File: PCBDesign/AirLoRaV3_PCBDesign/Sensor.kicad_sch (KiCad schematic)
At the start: 11 parts, among them J3 UART2, J4 UART2, J5 UART2, Q1 S8050, Q2 S8050, Q3 S8050, Q4 S8050, U5 SHT21

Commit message: Update circiut
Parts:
- added R12, R13, R14, R15: 1K, Resistor_SMD:R_0603_1608Metric, symbol Device:R
- C41: footprint (none) -> Capacitor_SMD:C_0603_1608Metric
- R10: renamed from R4; footprint (none) -> Resistor_SMD:R_0603_1608Metric
- R11: renamed from R5; footprint (none) -> Resistor_SMD:R_0603_1608Metric
- U5: footprint SHT21:XDCR_SHT21 -> footprint:XDCR_SHT21
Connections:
- net GND: now also Q1.1 (E); no longer C41.2, U5.2 (VSS)
- net at Q3.2 (B): now also R14.2
- net at Q2.2 (B): now also R13.2
- net at Q2.3 (C): now also J3.2 (Pin_2)
- net at Q1.2 (B): now also R12.1
- net at Q1.3 (C): now also C41.2, U5.2 (VSS)
- net at Q4.2 (B): now also R15.2
- net 3.3V renamed +3.3V
- net 5V renamed +5V
- new net EN_CO: R15.1
- new net EN_N02: R14.1
- new net EN_PM: R13.1
- new net EN_SHT: R12.2
- no-connect marks 1 -> 2
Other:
- moved on the sheet: C41, J3, J4, J5, Q1, Q2, Q3, Q4, R10, R11, U5

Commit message: Update PCB layout
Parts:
- removed C41: 100nF, Capacitor_SMD:C_0603_1608Metric, symbol Device:C
- removed R10, R11: 10K, Resistor_SMD:R_0603_1608Metric, symbol Device:R
- removed U5: SHT21, footprint:XDCR_SHT21, symbol SHT21:SHT21
- added J3: DHT, Connector_JST:JST_XH_B3B-XH-A_1x03_P2.50mm_Vertical, symbol Connector:Screw_Terminal_01x03
- J4: renamed from J3; value UART2 -> UART1
- J6: renamed from J5; value UART2 -> I2C
- Q1, Q2, Q3, Q4: footprint Package_TO_SOT_THT:TO-92_Inline -> Package_TO_SOT_SMD:SOT-23
- renumbered J4 to J5, R12 to R14, R13 to R15, R14 to R16, R15 to R17
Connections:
- net +5V: now also J3.1 (Pin_1)
- net RX_NO2: now also J5.4 (Pin_4); no longer J5.3 (Pin_3)
- net TX_NO2: now also J5.3 (Pin_3); no longer J5.4 (Pin_4)
- net at Q1.3 (C): now also J3.3 (Pin_3)
- new net DHT: J3.2 (Pin_2)
- no-connect marks 2 -> 0
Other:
- note added: "Temperature DHT Sensor"
- note removed: "Temperature SHT21 Sensor"
- moved on the sheet: Q1, R14

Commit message: update
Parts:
- added C41: 0.1uF, Capacitor_SMD:C_0603_1608Metric, symbol Device:C
- added R13: 1K, Resistor_SMD:R_0603_1608Metric, symbol Device:R
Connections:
- net +5V: now also C41.1
- net DHT: now also R13.1
- net at J3.3 (Pin_3), Q1.3 (C): now also C41.2, R13.2

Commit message: Update schematic
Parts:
- renumbered C41 to C36, J3 to J4, J4 to J5, J5 to J6, J6 to J7, Q1 to Q2, Q2 to Q3, Q3 to Q4, Q4 to Q5, R13 to R14, R14 to R15, R15 to R16, R16 to R17, R17 to R18
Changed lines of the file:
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@@
 		(on_board yes)
 		(dnp no)
-		(property "Reference" "#PWR040"
+		(property "Reference" "#PWR042"
 			(at 214.63 100.33 0)
 			(effects
@@
 			(project "airlora-kicad"
 				(path "/59d971df-d6c1-4ef7-a085-bf08b7b16047/be77b740-d58b-414b-97ce-61f1d1685314/51adec1c-c556-4645-b650-96b50e0dcbbc"
-					(reference "#PWR040")
+					(reference "#PWR042")
 					(unit 1)
 				)
@@
 		(on_board yes)
 		(dnp no)
-		(property "Reference" "#PWR036"
+		(property "Reference" "#PWR038"
 			(at 88.9 111.76 0)
 			(effects
@@
 			(project "airlora-kicad"
 				(path "/59d971df-d6c1-4ef7-a085-bf08b7b16047/be77b740-d58b-414b-97ce-61f1d1685314/51adec1c-c556-4645-b650-96b50e0dcbbc"
-					(reference "#PWR036")
+					(reference "#PWR038")
 					(unit 1)
 				)
@@
 		(on_board yes)
 		(dnp no)
-		(property "Reference" "R13"
+		(property "Reference" "R14"
 			(at 61.214 89.154 90)
 			(effects
@@
 			(project "airlora-kicad"
 				(path "/59d971df-d6c1-4ef7-a085-bf08b7b16047/be77b740-d58b-414b-97ce-61f1d1685314/51adec1c-c556-4645-b650-96b50e0dcbbc"
-					(reference "R13")
+					(reference "R14")
 					(unit 1)
 				)
@@
 		(on_board yes)
 		(dnp no)
-		(property "Reference" "#PWR038"
+		(property "Reference" "#PWR040"
 			(at 162.56 100.33 0)
 			(effects
@@
 			(project "airlora-kicad"
 				(path "/59d971df-d6c1-4ef7-a085-bf08b7b16047/be77b740-d58b-414b-97ce-61f1d1685314/51adec1c-c556-4645-b650-96b50e0dcbbc"
-					(reference "#PWR038")
+					(reference "#PWR040")
 					(unit 1)
 				)
@@
 		(on_board yes)
 		(dnp no)
-		(property "Reference" "#PWR035"
+		(property "Reference" "#PWR037"
 			(at 76.2 92.71 0)
 			(effects
@@
 			(project "airlora-kicad"
 				(path "/59d971df-d6c1-4ef7-a085-bf08b7b16047/be77b740-d58b-414b-97ce-61f1d1685314/51adec1c-c556-4645-b650-96b50e0dcbbc"
-					(reference "#PWR035")
+					(reference "#PWR037")
 					(unit 1)
 				)
@@
 		(dnp no)
 		(fields_autoplaced yes)
-		(property "Reference" "J6"
+		(property "Reference" "J7"
 			(at 246.38 82.55 0)
 			(effects
@@
 			(project "airlora-kicad"
 				(path "/59d971df-d6c1-4ef7-a085-bf08b7b16047/be77b740-d58b-414b-97ce-61f1d1685314/51adec1c-c556-4645-b650-96b50e0dcbbc"
-					(reference "J6")
+					(reference "J7")
 					(unit 1)
 				)
@@
 		(dnp no)
 		(fields_autoplaced yes)
-		(property "Reference" "Q3"
+		(property "Reference" "Q4"
 			(at 199.39 104.1399 0)
 			(effects
@@
 			(project "airlora-kicad"
 				(path "/59d971df-d6c1-4ef7-a085-bf08b7b16047/be77b740-d58b-414b-97ce-61f1d1685314/51adec1c-c556-4645-b650-96b50e0dcbbc"
-					(reference "Q3")
+					(reference "Q4")
 					(unit 1)
 				)
@@
 		(dnp no)
 		(fields_autoplaced yes)
-		(property "Reference" "J5"
+		(property "Reference" "J6"
 			(at 196.85 82.55 0)
 			(effects
@@
 			(project "airlora-kicad"
 				(path "/59d971df-d6c1-4ef7-a085-bf08b7b16047/be77b740-d58b-414b-97ce-61f1d1685314/51adec1c-c556-4645-b650-96b50e0dcbbc"
-					(reference "J5")
+					(reference "J6")
 					(unit 1)
 				)
@@
 		(on_board yes)
 		(dnp no)
-		(property "Reference" "R15"
+		(property "Reference" "R16"
 			(at 137.414 101.854 90)
 			(effects
@@
 			(project "airlora-kicad"
 				(path "/59d971df-d6c1-4ef7-a085-bf08b7b16047/be77b740-d58b-414b-97ce-61f1d1685314/51adec1c-c556-4645-b650-96b50e0dcbbc"
-					(reference "R15")
+					(reference "R16")
 					(unit 1)
 				)
@@
 		(on_board yes)
 		(dnp no)
-		(property "Reference" "#PWR039"
+		(property "Reference" "#PWR041"
 			(at 203.2 110.49 0)
 			(effects
@@
 			(project "airlora-kicad"
 				(path "/59d971df-d6c1-4ef7-a085-bf08b7b16047/be77b740-d58b-414b-97ce-61f1d1685314/51adec1c-c556-4645-b650-96b50e0dcbbc"
-					(reference "#PWR039")
+					(reference "#PWR041")
 					(unit 1)
 				)
@@
 		(on_board yes)
 		(dnp no)
-		(property "Reference" "#PWR037"
+		(property "Reference" "#PWR039"
 			(at 153.67 110.49 0)
 			(effects
@@
 			(project "airlora-kicad"
 				(path "/59d971df-d6c1-4ef7-a085-bf08b7b16047/be77b740-d58b-414b-97ce-61f1d1685314/51adec1c-c556-4645-b650-96b50e0dcbbc"
-					(reference "#PWR037")
+					(reference "#PWR039")
 					(unit 1)
 				)
@@
 		(dnp no)
 		(fields_autoplaced yes)
-		(property "Reference" "Q2"
+		(property "Reference" "Q3"
 			(at 149.86 104.1399 0)
 			(effects
@@
 			(project "airlora-kicad"
 				(path "/59d971df-d6c1-4ef7-a085-bf08b7b16047/be77b740-d58b-414b-97ce-61f1d1685314/51adec1c-c556-4645-b650-96b50e0dcbbc"
-					(reference "Q2")
+					(reference "Q3")
 					(unit 1)
 				)
@@
 		(dnp no)
 		(fields_autoplaced yes)
-		(property "Reference" "J3"
+		(property "Reference" "J4"
 			(at 67.31 86.36 0)
 			(effects
@@
 			(project "airlora-kicad"
 				(path "/59d971df-d6c1-4ef7-a085-bf08b7b16047/be77b740-d58b-414b-97ce-61f1d1685314/51adec1c-c556-4645-b650-96b50e0dcbbc"
-					(reference "J3")
+					(reference "J4")
 					(unit 1)
 				)
@@
 		(on_board yes)
 		(dnp no)
-		(property "Reference" "C41"
+		(property "Reference" "C36"
 			(at 62.738 101.854 90)
 			(effects
@@
 			(project "airlora-kicad"
 				(path "/59d971df-d6c1-4ef7-a085-bf08b7b16047/be77b740-d58b-414b-97ce-61f1d1685314/51adec1c-c556-4645-b650-96b50e0dcbbc"
-					(reference "C41")
+					(reference "C36")
 					(unit 1)
 				)
@@
 		(dnp no)
 		(fields_autoplaced yes)
-		(property "Reference" "Q1"
+		(property "Reference" "Q2"
 			(at 91.44 99.0599 0)
 			(effects
@@
 			(project "airlora-kicad"
 				(path "/59d971df-d6c1-4ef7-a085-bf08b7b16047/be77b740-d58b-414b-97ce-61f1d1685314/51adec1c-c556-4645-b650-96b50e0dcbbc"
-					(reference "Q1")
+					(reference "Q2")
 					(unit 1)
 				)
@@
 		(on_board yes)
 		(dnp no)
-		(property "Reference" "R14"
+		(property "Reference" "R15"
 			(at 86.614 85.344 90)
 			(effects
@@
 			(project "airlora-kicad"
 				(path "/59d971df-d6c1-4ef7-a085-bf08b7b16047/be77b740-d58b-414b-97ce-61f1d1685314/51adec1c-c556-4645-b650-96b50e0dcbbc"
-					(reference "R14")
+					(reference "R15")
 					(unit 1)
 				)
@@
 		(on_board yes)
 		(dnp no)
-		(property "Reference" "R17"
+		(property "Reference" "R18"
 			(at 236.474 101.854 90)
 			(effects
@@
 			(project "airlora-kicad"
 				(path "/59d971df-d6c1-4ef7-a085-bf08b7b16047/be77b740-d58b-414b-97ce-61f1d1685314/51adec1c-c556-4645-b650-96b50e0dcbbc"
-					(reference "R17")
+					(reference "R18")
 					(unit 1)
 				)
@@
 		(dnp no)
 		(fields_autoplaced yes)
-		(property "Reference" "Q4"
+		(property "Reference" "Q5"
 			(at 248.92 104.1399 0)
 			(effects
@@
 			(project "airlora-kicad"
 				(path "/59d971df-d6c1-4ef7-a085-bf08b7b16047/be77b740-d58b-414b-97ce-61f1d1685314/51adec1c-c556-4645-b650-96b50e0dcbbc"
-					(reference "Q4")
+					(reference "Q5")
 					(unit 1)
 				)
@@
 		(dnp no)
 		(fields_autoplaced yes)
-		(property "Reference" "J4"
+		(property "Reference" "J5"
 			(at 147.32 82.55 0)
 			(effects
@@
 			(project "airlora-kicad"
 				(path "/59d971df-d6c1-4ef7-a085-bf08b7b16047/be77b740-d58b-414b-97ce-61f1d1685314/51adec1c-c556-4645-b650-96b50e0dcbbc"
-					(reference "J4")
+					(reference "J5")
 					(unit 1)
 				)
@@
 		(on_board yes)
 		(dnp no)
-		(property "Reference" "#PWR042"
+		(property "Reference" "#PWR044"
 			(at 265.43 100.33 0)
 			(effects
@@
 			(project "airlora-kicad"
 				(path "/59d971df-d6c1-4ef7-a085-bf08b7b16047/be77b740-d58b-414b-97ce-61f1d1685314/51adec1c-c556-4645-b650-96b50e0dcbbc"
-					(reference "#PWR042")
+					(reference "#PWR044")
 					(unit 1)
 				)
@@
 		(on_board yes)
 		(dnp no)
-		(property "Reference" "R16"
+		(property "Reference" "R17"
 			(at 186.944 101.854 90)
 			(effects
@@
 			(project "airlora-kicad"
 				(path "/59d971df-d6c1-4ef7-a085-bf08b7b16047/be77b740-d58b-414b-97ce-61f1d1685314/51adec1c-c556-4645-b650-96b50e0dcbbc"
-					(reference "R16")
+					(reference "R17")
 					(unit 1)
 				)
@@
 		(on_board yes)
 		(dnp no)
-		(property "Reference" "#PWR041"
+		(property "Reference" "#PWR043"
 			(at 252.73 110.49 0)
 			(effects
@@
 			(project "airlora-kicad"
 				(path "/59d971df-d6c1-4ef7-a085-bf08b7b16047/be77b740-d58b-414b-97ce-61f1d1685314/51adec1c-c556-4645-b650-96b50e0dcbbc"
-					(reference "#PWR041")
-					(unit 1)
-				)
+					(reference "#PWR043")
+					(unit 1)
+				)

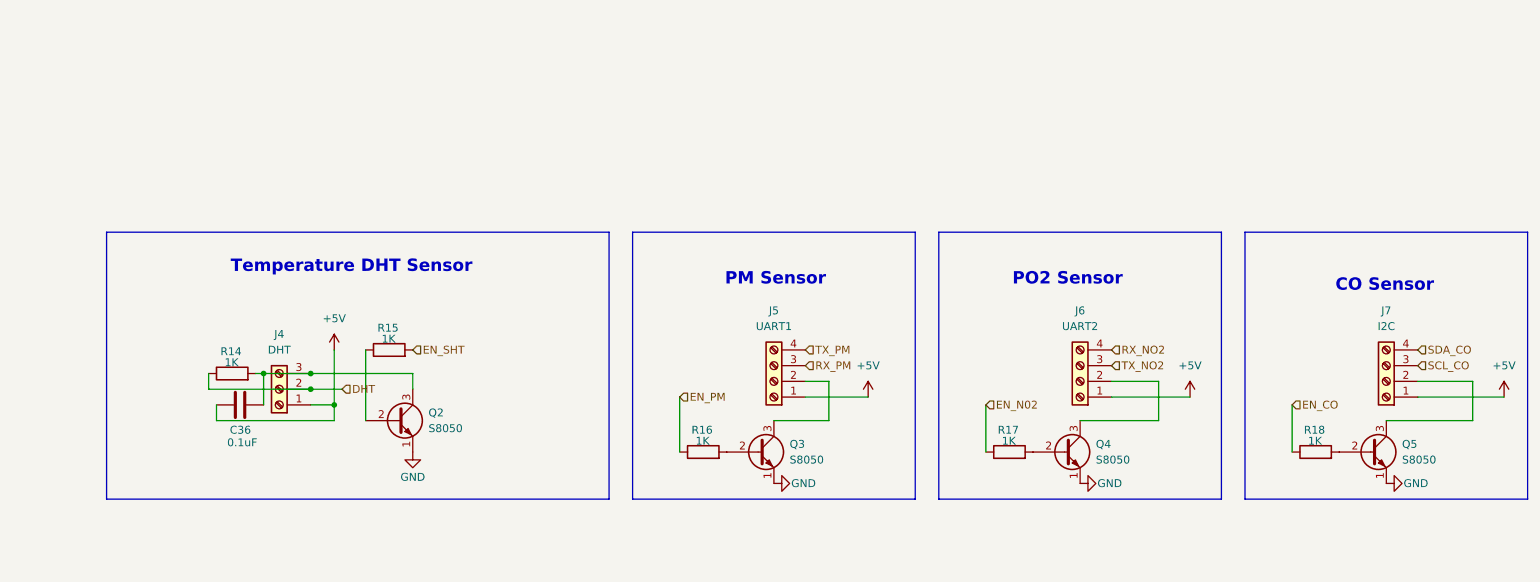
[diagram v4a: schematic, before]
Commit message: Update circuit buck converter and sensor
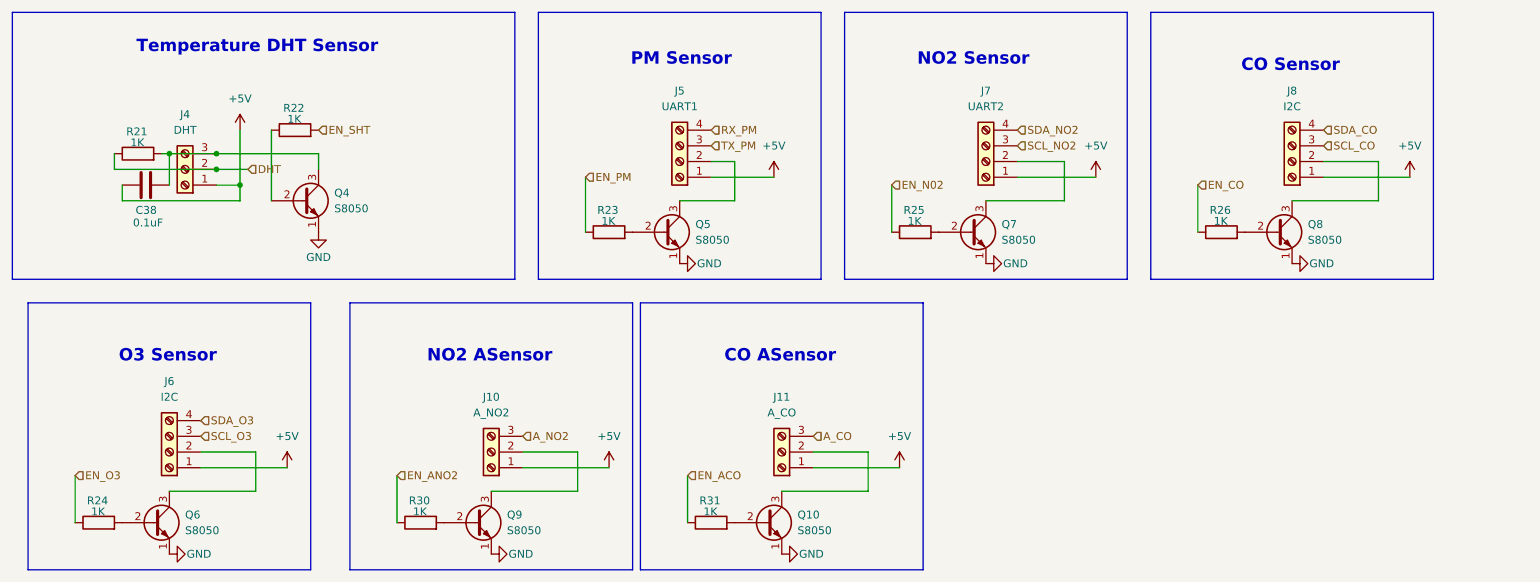
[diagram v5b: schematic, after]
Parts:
- added J10: A_NO2, Connector_Molex:Molex_CLIK-Mate_502585-0370_1x03-1MP_P1.50mm_Horizontal, symbol Connector:Screw_Terminal_01x03
- added J11: A_CO, Connector_Molex:Molex_CLIK-Mate_502585-0370_1x03-1MP_P1.50mm_Horizontal, symbol Connector:Screw_Terminal_01x03
- added J6: I2C, Connector_Molex:Molex_CLIK-Mate_502585-0470_1x04-1MP_P1.50mm_Horizontal, symbol Connector:Screw_Terminal_01x04
- added Q10, Q6, Q9: S8050, Package_TO_SOT_SMD:SOT-23, symbol Transistor_BJT:S8050
- added R24, R30, R31: 1K, Resistor_SMD:R_0603_1608Metric, symbol Device:R
- J4: footprint Connector_JST:JST_XH_B3B-XH-A_1x03_P2.50mm_Vertical -> Connector_Molex:Molex_CLIK-Mate_502585-0370_1x03-1MP_P1.50mm_Horizontal
- J5: footprint Connector_JST:JST_XH_B4B-XH-A_1x04_P2.50mm_Vertical -> Connector_Molex:Molex_CLIK-Mate_502585-0470_1x04-1MP_P1.50mm_Horizontal
- J7: renamed from J6; footprint Connector_JST:JST_XH_B4B-XH-A_1x04_P2.50mm_Vertical -> Connector_Molex:Molex_CLIK-Mate_502585-0470_1x04-1MP_P1.50mm_Horizontal
- J8: renamed from J7; footprint Connector_JST:JST_XH_B4B-XH-A_1x04_P2.50mm_Vertical -> Connector_Molex:Molex_CLIK-Mate_502585-0470_1x04-1MP_P1.50mm_Horizontal
- renumbered C36 to C38, Q2 to Q4, Q3 to Q5, Q4 to Q7, Q5 to Q8, R14 to R21, R15 to R22, R16 to R23, R17 to R25, R18 to R26
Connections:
- net +5V: now also J10.1 (Pin_1), J11.1 (Pin_1), J6.1 (Pin_1)
- net GND: now also Q10.1 (E), Q6.1 (E), Q9.1 (E)
- net RX_PM: now also J5.4 (Pin_4); no longer J5.3 (Pin_3)
- net TX_PM: now also J5.3 (Pin_3); no longer J5.4 (Pin_4)
- net RX_NO2 renamed SDA_NO2
- net TX_NO2 renamed SCL_NO2
- new net: Q6.2 (B), R24.2
- new net: J6.2 (Pin_2), Q6.3 (C)
- new net: Q10.2 (B), R31.2
- new net: J11.2 (Pin_2), Q10.3 (C)
- new net: Q9.2 (B), R30.2
- new net: J10.2 (Pin_2), Q9.3 (C)
- new net A_CO: J11.3 (Pin_3)
- new net A_NO2: J10.3 (Pin_3)
- new net EN_ACO: R31.1
- new net EN_ANO2: R30.1
- new net EN_O3: R24.1
- new net SCL_O3: J6.3 (Pin_3)
- new net SDA_O3: J6.4 (Pin_4)
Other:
- note added: "CO ASensor"
- note added: "NO2 ASensor"
- note added: "NO2 Sensor"
- note added: "O3 Sensor"
- note removed: "PO2 Sensor"
- moved on the sheet: C38, J4, J5, J7, J8, Q4, Q5, Q7, Q8, R21, R22, R23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

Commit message: Update schematic
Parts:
- removed C38: 0.1uF, Capacitor_SMD:C_0603_1608Metric, symbol Device:C
- removed J4: DHT, Connector_Molex:Molex_CLIK-Mate_502585-0370_1x03-1MP_P1.50mm_Horizontal, symbol Connector:Screw_Terminal_01x03
- removed R21: 1K, Resistor_SMD:R_0603_1608Metric, symbol Device:R
- added J12: SHT, Connector_JST:JST_XH_B4B-XH-A_1x04_P2.50mm_Vertical, symbol Connector:Screw_Terminal_01x04
- J10, J11: footprint Connector_Molex:Molex_CLIK-Mate_502585-0370_1x03-1MP_P1.50mm_Horizontal -> Connector_JST:JST_XH_B3B-XH-A_1x03_P2.50mm_Vertical
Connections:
- net +5V: now also J12.1 (Pin_1)
- net at Q4.3 (C): now also J12.2 (Pin_2)
- new net SCL_SHT: J12.3 (Pin_3)
- new net SDA_SHT: J12.4 (Pin_4)
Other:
- note added: "Temperature SHT Sensor"
- note removed: "Temperature DHT Sensor"

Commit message: Update PCB
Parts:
- J9: renamed from J7; value UART2 -> I2C
- renumbered J8 to J10, J12 to J4, J6 to J5, J10 to J6, J5 to J7, J11 to J8, Q8 to Q10, Q6 to Q4, Q4 to Q5, Q9 to Q6, Q5 to Q7, Q10 to Q8, Q7 to Q9, R24 to R21, R30 to R23, R23 to R24, R31 to R25, R25 to R26, R26 to R27

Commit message: Update package and placement components
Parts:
- R21, R22, R23, R24, R25, R26, R27: footprint Resistor_SMD:R_0603_1608Metric -> Resistor_SMD:R_0402_1005Metric_Pad0.72x0.64mm_HandSolder
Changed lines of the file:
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@@
 			)
 		)
-		(property "Footprint" "Resistor_SMD:R_0603_1608Metric"
+		(property "Footprint" "Resistor_SMD:R_0402_1005Metric_Pad0.72x0.64mm_HandSolder"
 			(at 90.17 118.618 90)
 			(effects
@@
 			)
 		)
-		(property "Footprint" "Resistor_SMD:R_0603_1608Metric"
+		(property "Footprint" "Resistor_SMD:R_0402_1005Metric_Pad0.72x0.64mm_HandSolder"
 			(at 120.65 71.628 90)
 			(effects
@@
 			)
 		)
-		(property "Footprint" "Resistor_SMD:R_0603_1608Metric"
+		(property "Footprint" "Resistor_SMD:R_0402_1005Metric_Pad0.72x0.64mm_HandSolder"
 			(at 137.16 118.618 90)
 			(effects
@@
 			)
 		)
-		(property "Footprint" "Resistor_SMD:R_0603_1608Metric"
+		(property "Footprint" "Resistor_SMD:R_0402_1005Metric_Pad0.72x0.64mm_HandSolder"
 			(at 38.1 118.618 90)
 			(effects
@@
 			)
 		)
-		(property "Footprint" "Resistor_SMD:R_0603_1608Metric"
+		(property "Footprint" "Resistor_SMD:R_0402_1005Metric_Pad0.72x0.64mm_HandSolder"
 			(at 69.85 55.118 90)
 			(effects
@@
 			)
 		)
-		(property "Footprint" "Resistor_SMD:R_0603_1608Metric"
+		(property "Footprint" "Resistor_SMD:R_0402_1005Metric_Pad0.72x0.64mm_HandSolder"
 			(at 219.71 71.628 90)
 			(effects
@@
 			)
 		)
-		(property "Footprint" "Resistor_SMD:R_0603_1608Metric"
+		(property "Footprint" "Resistor_SMD:R_0402_1005Metric_Pad0.72x0.64mm_HandSolder"
 			(at 170.18 71.628 90)
 			(effects
